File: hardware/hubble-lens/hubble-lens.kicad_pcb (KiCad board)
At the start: 2 copper layers, 100 x 100 mm, 27 parts, among them J1 LEFT, J2 RIGHT, J3 SWD, J4 Left, J5 Bottom, J6 Right

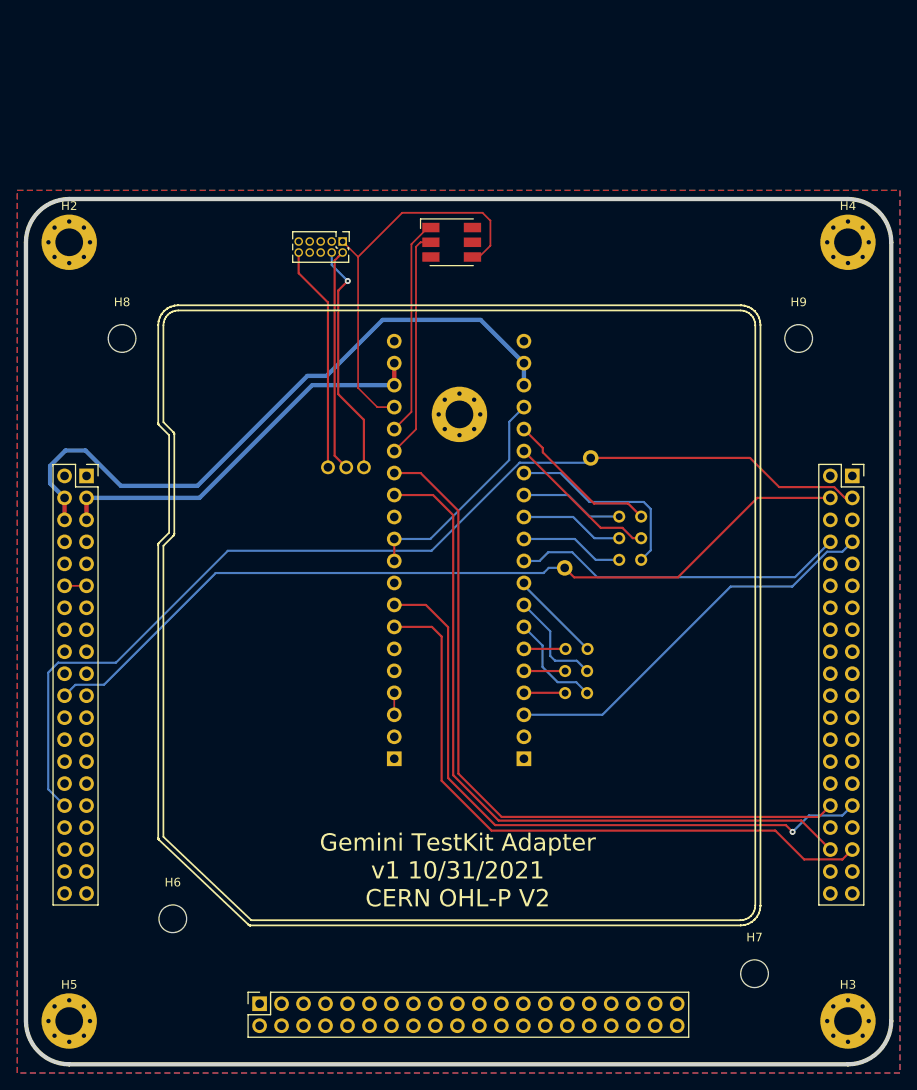
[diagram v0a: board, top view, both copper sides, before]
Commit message: hardware: Aadd expander and hubble lens
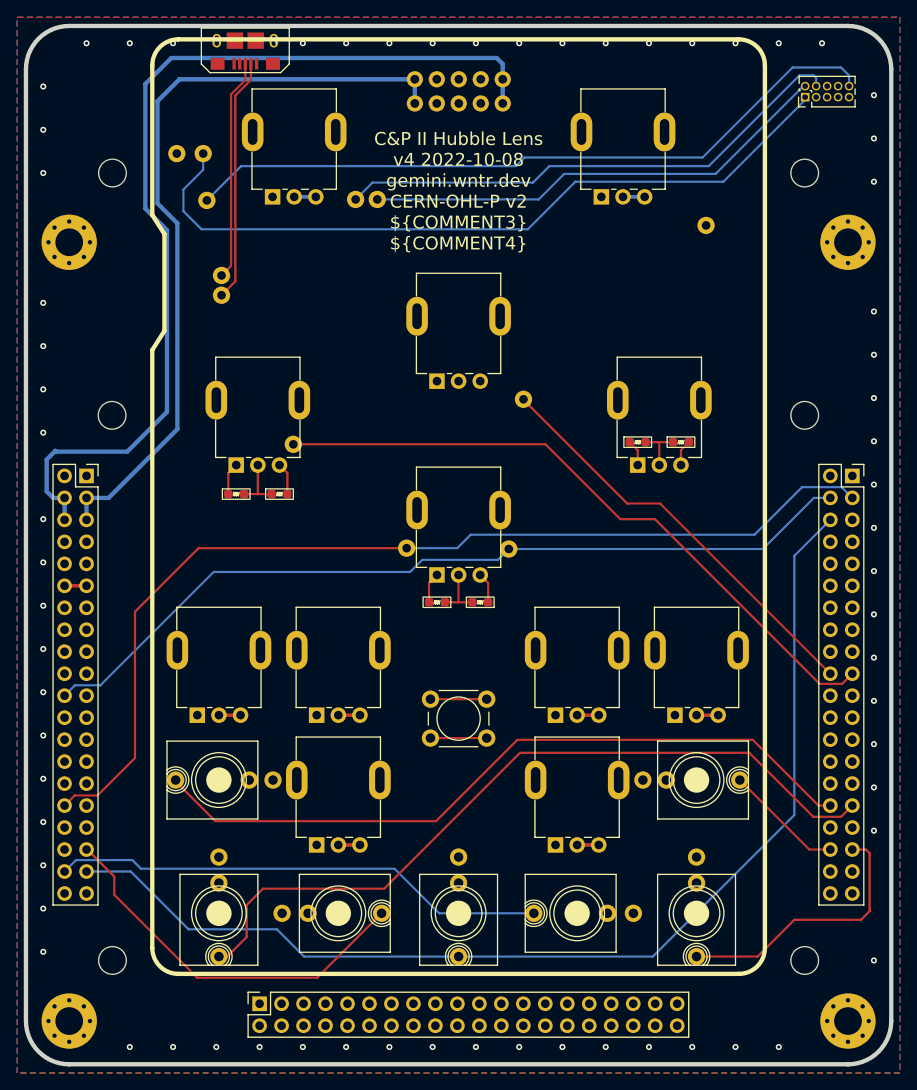
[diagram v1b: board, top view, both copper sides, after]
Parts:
- removed D1: DOTSTAR, LED_SMD:LED_RGB_5050-6
- removed J2: RIGHT, Connector_PinSocket_2.54mm:PinSocket_1x20_P2.54mm_Vertical
- removed JP1: P Ramp Mix, TestPoint:TestPoint_2Pads_Pitch2.54mm_Drill0.8mm
- removed JP2: P Pulse Mix, TestPoint:TestPoint_2Pads_Pitch2.54mm_Drill0.8mm
- removed JP3: P Sub Mix, TestPoint:TestPoint_2Pads_Pitch2.54mm_Drill0.8mm
- removed JP4: C Ramp Mix, TestPoint:TestPoint_2Pads_Pitch2.54mm_Drill0.8mm
- removed JP5: C Pulse Mix, TestPoint:TestPoint_2Pads_Pitch2.54mm_Drill0.8mm
- removed JP6: C Sub Mix, TestPoint:TestPoint_2Pads_Pitch2.54mm_Drill0.8mm
- added H10: M3, MountingHole:MountingHole_3.2mm_M3, F.Cu at (85.0, 74.0)
- added J10: MIX, winterbloom:AudioJack_WQP518MA, F.Cu at (125.0, 131.6)
- added J104: SWD, Connector_PinHeader_1.27mm:PinHeader_2x05_P1.27mm_Vertical, F.Cu at (165.1, 37.2)
- added J105: USB, winterbloom:USB_B_Micro_Receptacle, F.Cu at (100.5, 31.8)
- added J4: POLLUX PITCH, winterbloom:AudioJack_WQP518MA, F.Cu at (152.5, 131.6)
- added J5: CASTOR DUTY, winterbloom:AudioJack_WQP518MA, F.Cu at (97.3, 116.2)
- added J6: POLLUX DUTY, winterbloom:AudioJack_WQP518MA, F.Cu at (152.5, 116.2)
- added J7: CASTOR OUT, winterbloom:AudioJack_WQP518MA, F.Cu at (111.1, 131.6)
- added J8: POLLUX OUT, winterbloom:AudioJack_WQP518MA, F.Cu at (138.7, 131.6)
- added R1: 5k, winterbloom:R_0603_HandSolder, F.Cu at (104.3, 83.1)
- added R2: 5k, winterbloom:R_0603_HandSolder, F.Cu at (99.3, 83.1)
- added R3: 5k, winterbloom:R_0603_HandSolder, F.Cu at (150.7, 77.1)
- added R4: 5k, winterbloom:R_0603_HandSolder, F.Cu at (145.7, 77.1)
- added R5: 5k, winterbloom:R_0603_HandSolder, F.Cu at (122.5, 95.6)
- added R6: 5k, winterbloom:R_0603_HandSolder, F.Cu at (127.5, 95.6)
- added RV1: Castor pitch, winterbloom:Potentiometer_Alpha_R0904N, F.Cu at (106.0, 41.2)
- added RV10: Pulse level, winterbloom:Potentiometer_Alpha_R0904N, F.Cu at (138.7, 101.2)
- added RV11: Sub level, winterbloom:Potentiometer_Alpha_R0904N, F.Cu at (138.7, 116.2)
- added RV12: Crossfade, winterbloom:Potentiometer_Alpha_R0904N, F.Cu at (125.0, 85.0)
- added RV2: Pollux pitch, winterbloom:Potentiometer_Alpha_R0904N, F.Cu at (144.0, 41.2)
- added RV3: LFO, winterbloom:Potentiometer_Alpha_R0904N, F.Cu at (125.0, 62.5)
- added RV4: Castor duty, winterbloom:Potentiometer_Alpha_R0904N, F.Cu at (101.8, 72.2)
- added RV5: Pollux duty, winterbloom:Potentiometer_Alpha_R0904N, F.Cu at (148.2, 72.2)
- added RV6: Ramp level, winterbloom:Potentiometer_Alpha_R0904N, F.Cu at (97.3, 101.2)
- added RV7: Pulse level, winterbloom:Potentiometer_Alpha_R0904N, F.Cu at (111.1, 101.2)
- added RV8: Sub level, winterbloom:Potentiometer_Alpha_R0904N, F.Cu at (111.1, 116.2)
- added RV9: Ramp level, winterbloom:Potentiometer_Alpha_R0904N, F.Cu at (152.5, 101.2)
- added SW2: BUTTON, winterbloom:Tactile_Switch_6mm, F.Cu at (125.0, 109.0)
- added TP10: D-, TestPoint:TestPoint_THTPad_D2.0mm_Drill1.0mm, B.Cu at (97.6, 60.1)
- added TP11: Ramp A, TestPoint:TestPoint_THTPad_D2.0mm_Drill1.0mm, B.Cu at (119.0, 89.3)
- added TP12: Ramp B, TestPoint:TestPoint_THTPad_D2.0mm_Drill1.0mm, B.Cu at (130.8, 89.5)
- added TP6: RESET, TestPoint:TestPoint_THTPad_D2.0mm_Drill1.0mm, B.Cu at (95.9, 49.2)
- added TP7: SQ1, TestPoint:TestPoint_THTPad_D2.0mm_Drill1.0mm, B.Cu at (105.9, 77.3)
- added TP8: SQ2, TestPoint:TestPoint_THTPad_D2.0mm_Drill1.0mm, B.Cu at (132.5, 72.2)
- added TP9: D+, TestPoint:TestPoint_THTPad_D2.0mm_Drill1.0mm, B.Cu at (97.6, 57.8)
- H1: footprint MountingHole:MountingHole_3.2mm_M3_Pad_Via -> MountingHole:MountingHole_3.2mm_M3; moved to F.Cu
- J1: value LEFT -> Eurorack Power; footprint Connector_PinSocket_2.54mm:PinSocket_1x20_P2.54mm_Vertical -> winterbloom:Eurorack_Power_2x5_Shrouded
- J3: value SWD -> CASTOR PITCH; footprint Connector_PinHeader_1.27mm:PinHeader_2x05_P1.27mm_Vertical -> winterbloom:AudioJack_WQP518MA
- TP1: value SWCLK -> 3V3; footprint TestPoint:TestPoint_THTPad_D1.5mm_Drill0.7mm -> TestPoint:TestPoint_THTPad_D2.0mm_Drill1.0mm
- TP2: value SWDIO -> GND; footprint TestPoint:TestPoint_THTPad_D1.5mm_Drill0.7mm -> TestPoint:TestPoint_THTPad_D2.0mm_Drill1.0mm
- TP3: value RESET -> -10V; footprint TestPoint:TestPoint_THTPad_D1.5mm_Drill0.7mm -> TestPoint:TestPoint_THTPad_D2.0mm_Drill1.0mm
- TP4: value CORE A -> SWDIO; footprint TestPoint:TestPoint_THTPad_D1.5mm_Drill0.7mm -> TestPoint:TestPoint_THTPad_D2.0mm_Drill1.0mm
- TP5: value CORE B -> SWCLK; footprint TestPoint:TestPoint_THTPad_D1.5mm_Drill0.7mm -> TestPoint:TestPoint_THTPad_D2.0mm_Drill1.0mm
- moved J3 78.9 mm to (97.3, 131.6), turned to 180 degrees
- moved J1 75.8 mm to (130.1, 38.0), turned to 180 degrees
- moved TP3 51.9 mm to (153.6, 52.0)
- moved TP5 49.0 mm to (113.1, 49.0)
- moved TP2 41.2 mm to (92.4, 43.8)
- moved TP1 40.7 mm to (95.5, 43.8)
- moved H1 39.9 mm to (165.0, 74.0), turned to 0 degrees
- moved TP4 38.7 mm to (115.6, 49.0), turned to 0 degrees
- moved H8 19.2 mm to (85.0, 46.0)
- moved H9 19.1 mm to (165.0, 46.0)
- moved H6 8.47 mm to (85.0, 137.0)
- moved H7 6.00 mm to (165.0, 137.0)
- renumbered J4 to J101, J5 to J102, J6 to J103
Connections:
- net Net-(J6-Pad21) renamed IO3
- net Net-(J6-Pad22) renamed IO4
- net Net-(J6-Pad23) renamed IO5
- J1 pad 1: GND -> -12V
- J1 pad 10: EXT_AUDIO_B -> +12V
- J1 pad 2: GND -> -12V
- J1 pad 3: EXT_AUDIO_A -> GND
- J1 pad 4: /castor_sub_mix_in -> GND
- J1 pad 5: /castor_pwm_mix_in -> GND
- J1 pad 6: /castor_ramp_mix_in -> GND
- J1 pad 7: /castor_sub -> GND
- J1 pad 8: /castor_pwm -> GND
- J1 pad 9: /castor_ramp -> +12V
- J101 pad 15: Net-(J4-Pad15) -> unconnected-(J101-Pad15)
- J101 pad 16: Net-(J4-Pad16) -> unconnected-(J101-Pad16)
- J101 pad 17: Net-(J4-Pad17) -> unconnected-(J101-Pad17)
- J101 pad 18: Net-(J4-Pad18) -> unconnected-(J101-Pad18)
- J101 pad 7: Net-(J4-Pad7) -> unconnected-(J101-Pad7)
- J101 pad 8: Net-(J4-Pad8) -> unconnected-(J101-Pad8)
- J102 pad 10: Net-(J5-Pad10) -> unconnected-(J102-Pad10)
- J102 pad 13: Net-(J5-Pad13) -> unconnected-(J102-Pad13)
- J102 pad 14: Net-(J5-Pad14) -> unconnected-(J102-Pad14)
- J102 pad 15: Net-(J5-Pad15) -> unconnected-(J102-Pad15)
- J102 pad 16: Net-(J5-Pad16) -> unconnected-(J102-Pad16)
- J102 pad 21: Net-(J5-Pad21) -> unconnected-(J102-Pad21)
- J102 pad 22: Net-(J5-Pad22) -> unconnected-(J102-Pad22)
- J102 pad 23: Net-(J5-Pad23) -> unconnected-(J102-Pad23)
- J102 pad 24: Net-(J5-Pad24) -> unconnected-(J102-Pad24)
- J102 pad 25: Net-(J5-Pad25) -> unconnected-(J102-Pad25)
- J102 pad 26: Net-(J5-Pad26) -> unconnected-(J102-Pad26)
- J102 pad 27: Net-(J5-Pad27) -> unconnected-(J102-Pad27)
- J102 pad 3: Net-(J5-Pad3) -> unconnected-(J102-Pad3)
- J102 pad 4: Net-(J5-Pad4) -> unconnected-(J102-Pad4)
- J102 pad 5: Net-(J5-Pad5) -> unconnected-(J102-Pad5)
- J102 pad 6: Net-(J5-Pad6) -> unconnected-(J102-Pad6)
- J102 pad 7: Net-(J5-Pad7) -> unconnected-(J102-Pad7)
- J102 pad 8: Net-(J5-Pad8) -> unconnected-(J102-Pad8)
- J102 pad 9: Net-(J5-Pad9) -> unconnected-(J102-Pad9)
- J103 pad 19: Net-(J6-Pad19) -> IO1
- J103 pad 20: Net-(J6-Pad20) -> IO2
- J103 pad 25: Net-(J6-Pad25) -> unconnected-(J103-Pad25)
- J103 pad 26: Net-(J6-Pad26) -> unconnected-(J103-Pad26)
- J103 pad 27: Net-(J6-Pad27) -> unconnected-(J103-Pad27)
- J103 pad 28: Net-(J6-Pad28) -> unconnected-(J103-Pad28)
- J103 pad 6: EXT_OSC_C -> ADC_2D
- TP1 pad 1: Net-(J3-Pad4) -> /board_3v3
- TP2 pad 1: Net-(J3-Pad2) -> GND
- TP3 pad 1: Net-(J3-Pad10) -> unconnected-(TP3-Pad1)
- TP4 pad 1: ADC_3A -> Net-(J104-Pad2)
- TP5 pad 1: ADC_1A -> Net-(J104-Pad4)
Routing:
- net ADC_2D: track 0.00 -> 128.5 mm
- net Net-(J104-Pad10): track 0.00 -> 82.2 mm
- net IO1: track 0.00 -> 76.6 mm
- net DAC_4A: track 85.0 -> 13.8 mm
- net Net-(J104-Pad4): track 0.00 -> 60.2 mm
- net ADC_2C: track 0.00 -> 57.3 mm
- net Net-(J104-Pad2): track 0.00 -> 54.9 mm
- net IO2: track 0.00 -> 48.6 mm
- net EXT_AUDIO_A: track 46.2 -> 0.00 mm
- net ADC_2B: track 0.00 -> 44.6 mm
- net DAC_4B: track 74.3 -> 31.0 mm
- net +12V: track 46.0 -> 88.8 mm
- net /board_3v3: track 46.1 -> 86.8 mm
- net EXT_AUDIO_B: track 38.7 -> 0.00 mm
- net -12V: track 76.7 -> 111.2 mm
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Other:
- board size 100 x 100 mm -> 100 x 120 mm
- net class 12V removed
- net class 3.3V removed
- net class Absolute minimum removed
- net class Analog removed
- net class Default removed
- board text added: "${TITLE} ${REVISION} ${ISSUE_DATE} ${COMMENT1} ${COMMENT2} ${COMMENT3} ${COMMENT4}"
- board text removed: "Gemini TestKit Adapter v1 10/31/2021 CERN OHL-P V2"
